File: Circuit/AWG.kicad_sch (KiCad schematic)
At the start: 24 parts, among them J1 Power, J2 Pump 1, J3 Pump 2, M1 Fan 1, M2 Fan 2, Q1 FQPF47P06, SW1 Switch, U1 R-78E5.0-0.5, U2 LM393

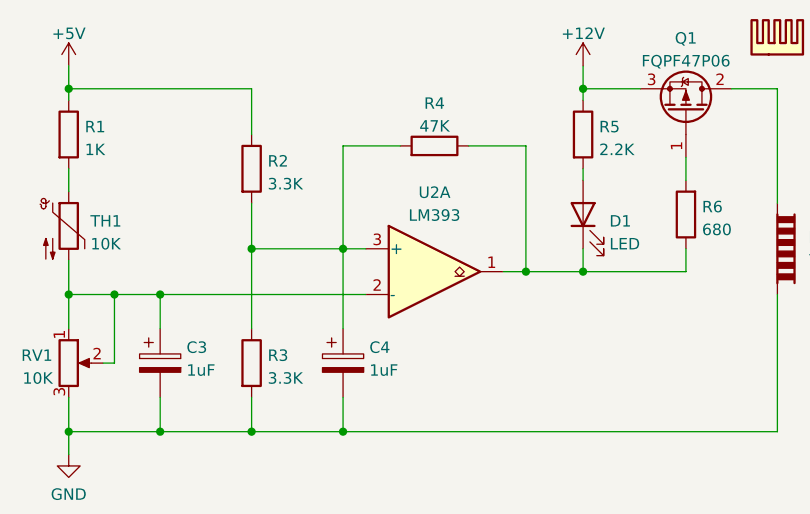
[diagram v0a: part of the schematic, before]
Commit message: [Circuit] Change a resistor to a potentiometer to adjust upper bound of the switching
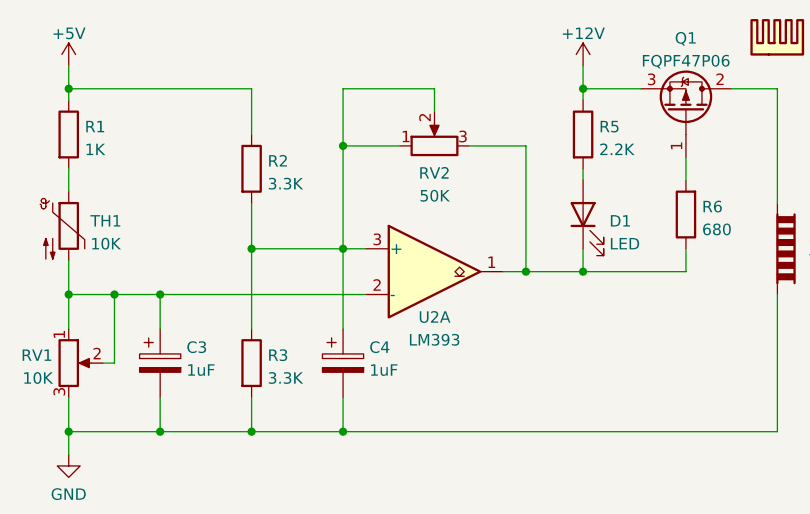
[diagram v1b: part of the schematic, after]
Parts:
- removed R4: 47K, Resistor_THT:R_Axial_DIN0207_L6.3mm_D2.5mm_P7.62mm_Horizontal, symbol Device:R
- added RV2: 50K, Potentiometer_THT:Potentiometer_Bourns_3339P_Vertical, symbol Device:R_Potentiometer
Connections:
- net at D1.1 (K), R6.1, U2.1: now also RV2.3
- net at C4.1, R2.2, R3.1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: now also RV2.1, RV2.2
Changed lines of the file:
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@@
   (junction (at 195.58 58.42) (diameter 0) (color 0 0 0 0)
+  )
+  (junction (at 175.26 44.45) (diameter 0) (color 0 0 0 0)
   )
   (junction (at 144.78 38.1) (diameter 0) (color 0 0 0 0)
@@
     (stroke (width 0) (type default) (color 0 0 0 0))
   )
+  (wire (pts (xy 185.42 38.1) (xy 175.26 38.1))
+    (stroke (width 0) (type default) (color 0 0 0 0))
+  )
   (wire (pts (xy 69.85 118.11) (xy 64.77 118.11))
     (stroke (width 0) (type default) (color 0 0 0 0))
@@
     (stroke (width 0) (type default) (color 0 0 0 0))
   )
+  (wire (pts (xy 185.42 40.64) (xy 185.42 38.1))
+    (stroke (width 0) (type default) (color 0 0 0 0))
+  )
   (wire (pts (xy 218.44 38.1) (xy 223.52 38.1))
     (stroke (width 0) (type default) (color 0 0 0 0))
@@
   )
   (wire (pts (xy 144.78 35.56) (xy 144.78 38.1))
+    (stroke (width 0) (type default) (color 0 0 0 0))
+  )
+  (wire (pts (xy 175.26 38.1) (xy 175.26 44.45))
     (stroke (width 0) (type default) (color 0 0 0 0))
   )
@@
     (pin "2")
   )
-  (symbol (lib_id "Device:R") (at 185.42 44.45 270) (mirror x) (unit 1)
-    (in_bom yes) (on_board yes) (fields_autoplaced)
-    (property "Reference" "R4" (id 0) (at 185.42 39.7342 90))
-    (property "Value" "47K" (id 1) (at 185.42 42.2711 90))
-    (property "Footprint" "Resistor_THT:R_Axial_DIN0207_L6.3mm_D2.5mm_P7.62mm_Horizontal" (id 2) (at 185.42 46.228 90)
-      (effects (font (size 1.27 1.27)) hide)
-    )
-    (property "Datasheet" "~" (id 3) (at 185.42 44.45 0)
-      (effects (font (size 1.27 1.27)) hide)
-    )
-    (pin "1")
-    (pin "2")
-  )
   (symbol (lib_id "Device:C_Polarized") (at 83.82 59.69 0) (mirror y) (unit 1)
     (in_bom yes) (on_board yes)
@@
   )
   (symbol (lib_id "Comparator:LM393") (at 185.42 58.42 0) (unit 1)
-    (in_bom yes) (on_board yes) (fields_autoplaced)
-    (property "Reference" "U2" (id 0) (at 185.42 49.6402 0))
-    (property "Value" "LM393" (id 1) (at 185.42 52.1771 0))
+    (in_bom yes) (on_board yes)
+    (property "Reference" "U2" (id 0) (at 185.42 63.5031 0))
+    (property "Value" "LM393" (id 1) (at 185.42 66.04 0))
     (property "Footprint" "Package_DIP:DIP-8_W7.62mm_Socket" (id 2) (at 185.42 58.42 0)
       (effects (font (size 1.27 1.27)) hide)
@@
     (pin "2")
   )
+  (symbol (lib_id "Device:R_Potentiometer") (at 185.42 44.45 90) (unit 1)
+    (in_bom yes) (on_board yes) (fields_autoplaced)
+    (property "Reference" "RV2" (id 0) (at 185.42 47.4964 90))
+    (property "Value" "50K" (id 1) (at 185.42 50.0333 90))
+    (property "Footprint" "Potentiometer_THT:Potentiometer_Bourns_3339P_Vertical" (id 2) (at 185.42 44.45 0)
+      (effects (font (size 1.27 1.27)) hide)
+    )
+    (property "Datasheet" "~" (id 3) (at 185.42 44.45 0)
+      (effects (font (size 1.27 1.27)) hide)
+    )
+    (pin "1")
+    (pin "2")
+    (pin "3")
+  )
   (sheet_instances
     (path "/" (page "1"))
@@
       (reference "R3") (unit 1) (value "3.3K") (footprint "Resistor_THT:R_Axial_DIN0207_L6.3mm_D2.5mm_P7.62mm_Horizontal")
     )
-    (path "/1870fe66-613a-4315-8238-19d41d32004b"
-      (reference "R4") (unit 1) (value "47K") (footprint "Resistor_THT:R_Axial_DIN0207_L6.3mm_D2.5mm_P7.62mm_Horizontal")
-    )
     (path "/22d073f7-e4a0-4cd4-a3b1-cf11aea04c7d"
       (reference "R5") (unit 1) (value "2.2K") (footprint "Resistor_THT:R_Axial_DIN0207_L6.3mm_D2.5mm_P7.62mm_Horizontal")
@@
       (reference "RV1") (unit 1) (value "10K") (footprint "Potentiometer_THT:Potentiometer_Bourns_3339P_Vertical")
     )
+    (path "/fe02be9d-6a84-4770-83b0-5b2bf60db1ec"
+      (reference "RV2") (unit 1) (value "50K") (footprint "Potentiometer_THT:Potentiometer_Bourns_3339P_Vertical")
+    )
     (path "/941be606-5dae-46f1-be50-e2701a32a3aa"

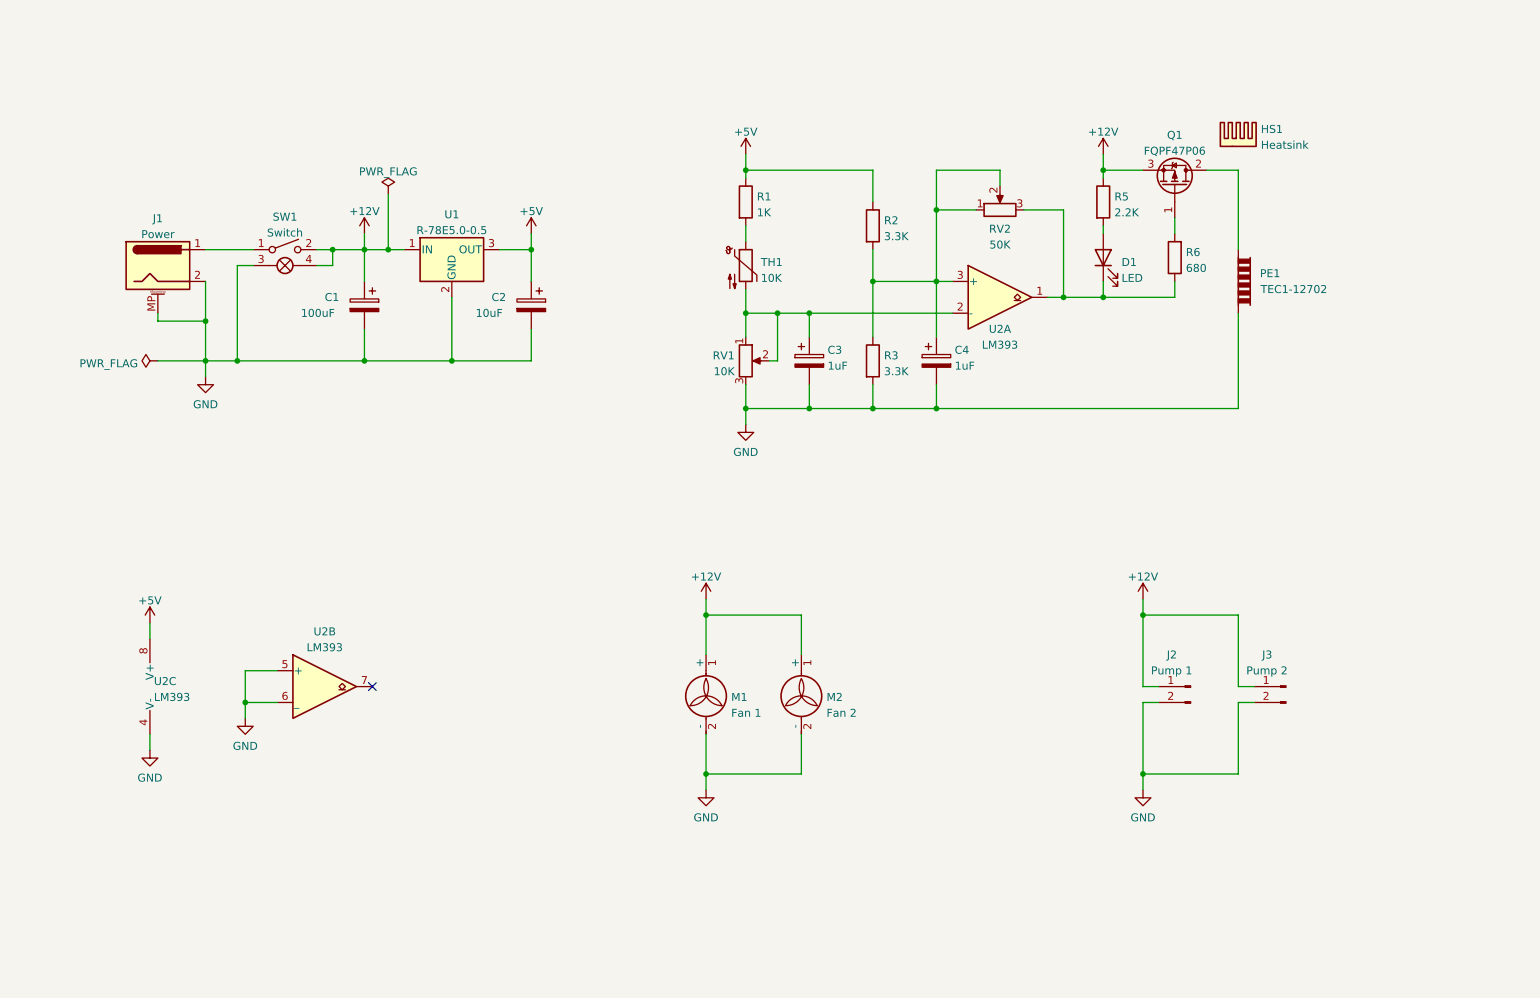
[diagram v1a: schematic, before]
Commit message: [Circuit] Redesign the control module, use an Arduino as the computation core
Related issue #6
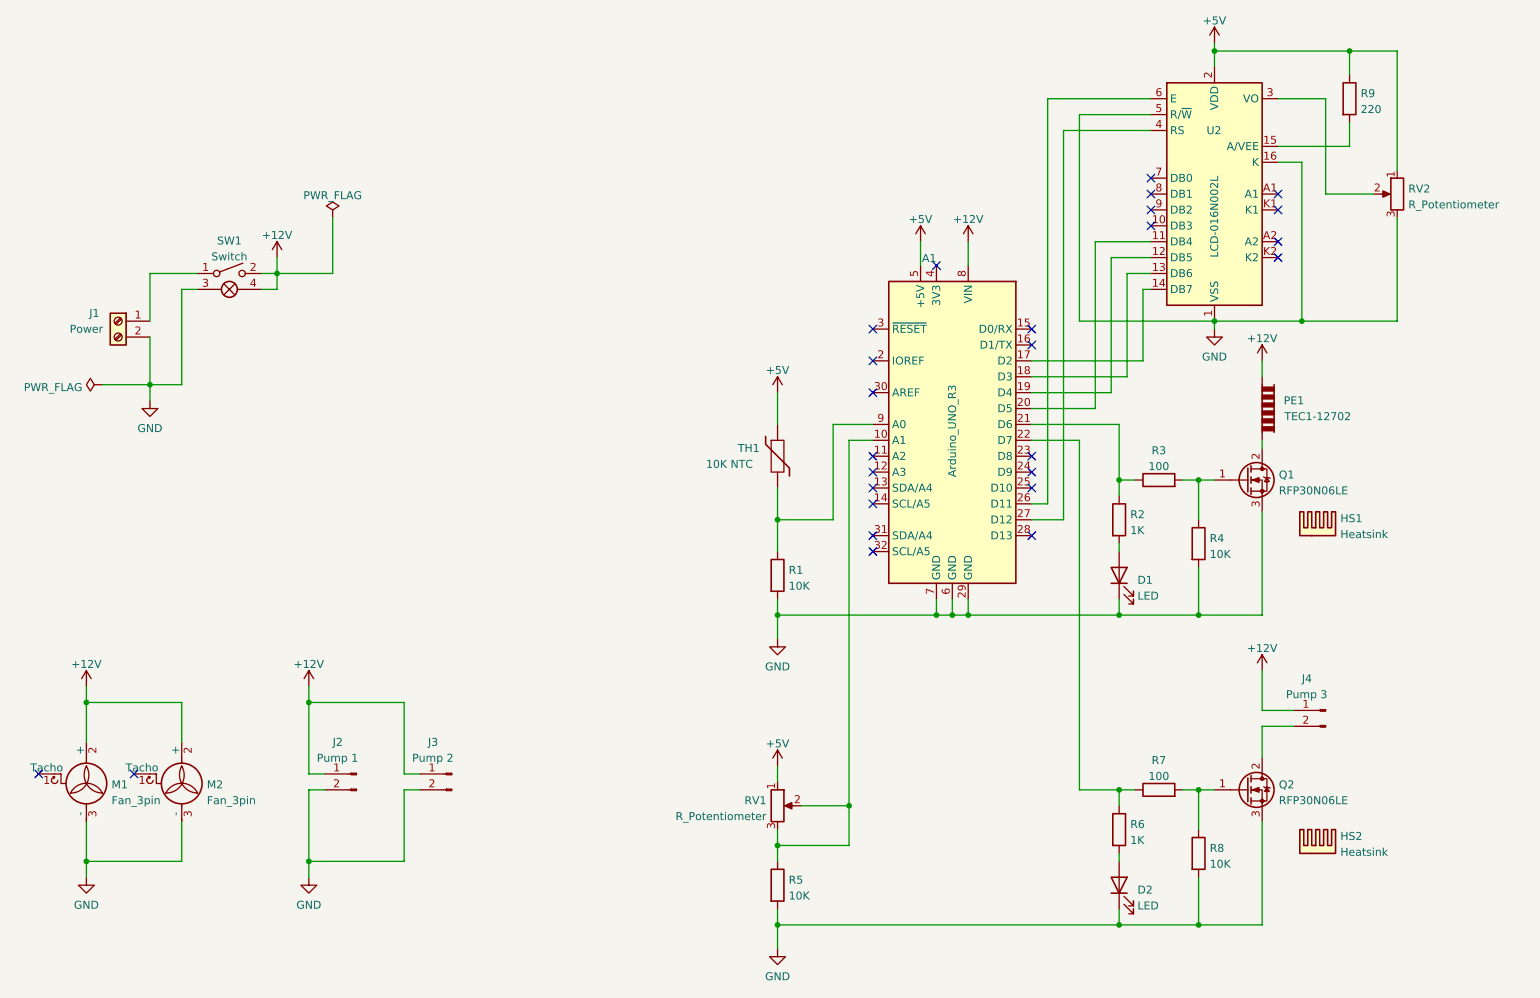
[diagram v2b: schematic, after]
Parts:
- removed C1: 100uF, Capacitor_THT:CP_Radial_D6.3mm_P2.50mm, symbol Device:C_Polarized
- removed C2: 10uF, Capacitor_THT:CP_Radial_D4.0mm_P1.50mm, symbol Device:C_Polarized
- removed C3, C4: 1uF, Capacitor_THT:CP_Radial_D4.0mm_P1.50mm, symbol Device:C_Polarized
- removed J1: Power, Connector_BarrelJack:BarrelJack_Wuerth_6941xx301002, symbol Connector:Barrel_Jack_MountingPin
- removed M1: Fan 1, Connector_JST:JST_XH_B2B-XH-A_1x02_P2.50mm_Vertical, symbol Motor:Fan
- removed M2: Fan 2, Connector_JST:JST_XH_B2B-XH-A_1x02_P2.50mm_Vertical, symbol Motor:Fan
- removed Q1: FQPF47P06, Package_TO_SOT_THT:TO-220-3_Vertical, symbol Device:Q_PMOS_GDS
- removed TH1: 10K, Connector_PinHeader_2.54mm:PinHeader_1x02_P2.54mm_Vertical, symbol Device:Thermistor_NTC
- removed U1: R-78E5.0-0.5, Converter_DCDC:Converter_DCDC_RECOM_R-78E-0.5_THT, symbol Regulator_Switching:R-78E5.0-0.5
- removed U2: LM393, Package_DIP:DIP-8_W7.62mm_Socket, symbol Comparator:LM393
- added A1: Arduino_UNO_R3, Module:Arduino_UNO_R3, symbol MCU_Module:Arduino_UNO_R3
- added D2: LED, LED_THT:LED_D3.0mm_FlatTop, symbol Device:LED
- added HS2: Heatsink, AWG:Heatsink_TO220_15x10mm, symbol Mechanical:Heatsink
- added J1: Power, TerminalBlock:TerminalBlock_bornier-2_P5.08mm, symbol Connector:Screw_Terminal_01x02
- added J4: Pump 3, Connector_PinHeader_2.54mm:PinHeader_1x02_P2.54mm_Vertical, symbol Connector:Conn_01x02_Male
- added M1, M2: Fan_3pin, Connector_PinHeader_2.54mm:PinHeader_1x03_P2.54mm_Vertical, symbol Motor:Fan_3pin
- added Q1, Q2: RFP30N06LE, Package_TO_SOT_THT:TO-220-3_Vertical, symbol Device:Q_NMOS_GDS
- added R4, R8: 10K, Resistor_THT:R_Axial_DIN0207_L6.3mm_D2.5mm_P7.62mm_Horizontal, symbol Device:R
- added R7: 100, Resistor_THT:R_Axial_DIN0207_L6.3mm_D2.5mm_P7.62mm_Horizontal, symbol Device:R
- added R9: 220, Resistor_THT:R_Axial_DIN0207_L6.3mm_D2.5mm_P7.62mm_Horizontal, symbol Device:R
- added TH1: 10K NTC, Connector_PinHeader_2.54mm:PinHeader_1x02_P2.54mm_Vertical, symbol Device:Thermistor
- added U2: LCD-016N002L, Display:LCD-016N002L, symbol Display_Character:LCD-016N002L
- J2, J3: footprint Connector_JST:JST_XH_B2B-XH-A_1x02_P2.50mm_Vertical -> Connector_PinHeader_2.54mm:PinHeader_1x02_P2.54mm_Vertical
- PE1: footprint Connector_JST:JST_XH_B2B-XH-A_1x02_P2.50mm_Vertical -> TerminalBlock:TerminalBlock_bornier-2_P5.08mm
- R1: value 1K -> 10K
- R2: value 3.3K -> 1K
- R3: value 3.3K -> 100
- R5: value 2.2K -> 10K
- R6: value 680 -> 1K
- RV1: value 10K -> R_Potentiometer; footprint Potentiometer_THT:Potentiometer_Bourns_3339P_Vertical -> (none)
- RV2: value 50K -> R_Potentiometer; footprint Potentiometer_THT:Potentiometer_Bourns_3339P_Vertical -> (none)
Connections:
- net +12V: now also PE1.2, A1.8 (VIN), J4.1 (Pin_1), M1.2 (+), M2.2 (+); no longer R5.1
- net +5V: now also RV1.1, RV2.1, A1.5 (+5V), R9.1, TH1.1, U2.2 (VDD); no longer R1.1, R2.1
- net GND: now also D1.1 (K), R1.2, R5.2, RV2.3, A1.29 (GND), A1.6 (GND), A1.7 (GND), D2.1 (K), J1.2 (Pin_2), M1.3 (-), M2.3 (-), Q1.3 (S), Q2.3 (S), R4.2, R8.2, U2.1 (VSS), U2.16 (K), U2.5 (R/~{W}); no longer PE1.2, R3.2, RV1.3
- net at D1.2 (A): now also R2.2; no longer R5.2
- net at SW1.1: now also J1.1 (Pin_1)
- net at PE1.1: now also Q1.2 (D)
- net at RV1.2: now also R5.1, RV1.3, A1.10 (A1); no longer RV1.1
- net at R6.2: now also D2.2 (A)
- new net: A1.17 (D2), U2.14 (DB7)
- new net: A1.18 (D3), U2.13 (DB6)
- new net: A1.19 (D4), U2.12 (DB5)
- new net: A1.20 (D5), U2.11 (DB4)
- new net: A1.21 (D6), R2.1, R3.1
- new net: A1.22 (D7), R6.1, R7.1
- new net: A1.26 (D11), U2.6 (E)
- new net: A1.27 (D12), U2.4 (RS)
- new net: A1.9 (A0), R1.1, TH1.2
- new net: Q1.1 (G), R3.2, R4.1
- new net: J4.2 (Pin_2), Q2.2 (D)
- new net: Q2.1 (G), R7.2, R8.1
- new net: R9.2, U2.15 (A/VEE)
- new net: RV2.2, U2.3 (VO)
- no-connect marks 1 -> 26

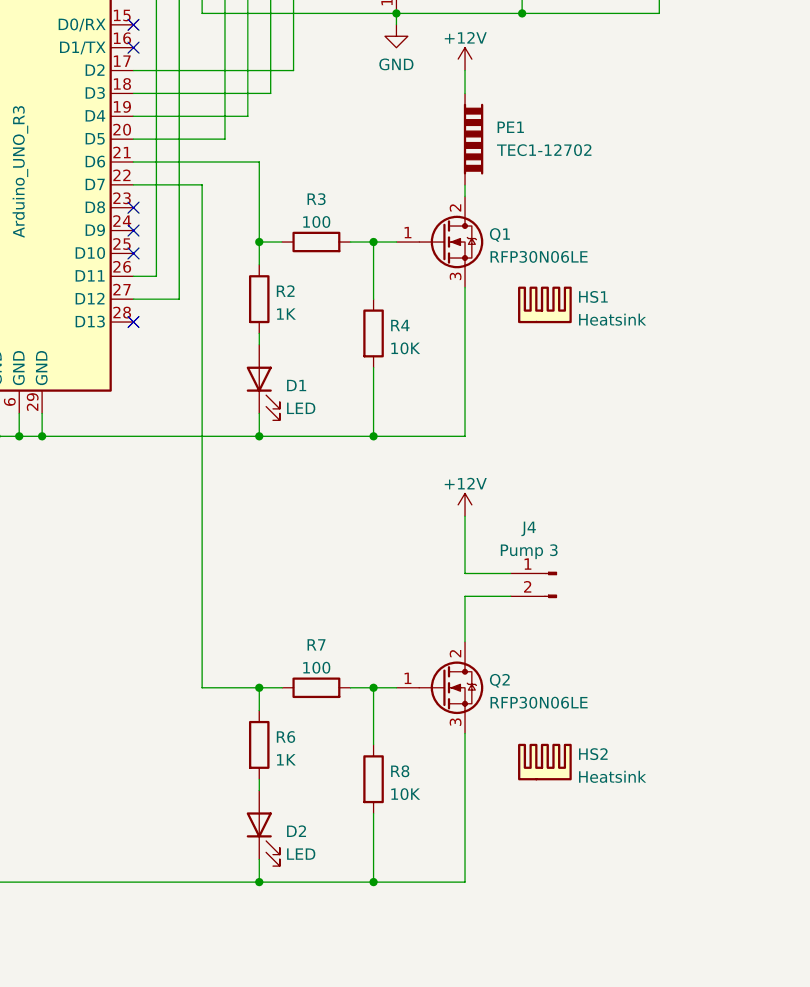
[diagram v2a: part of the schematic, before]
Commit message: [Circuit] Adjust the mosfet part in the circuit
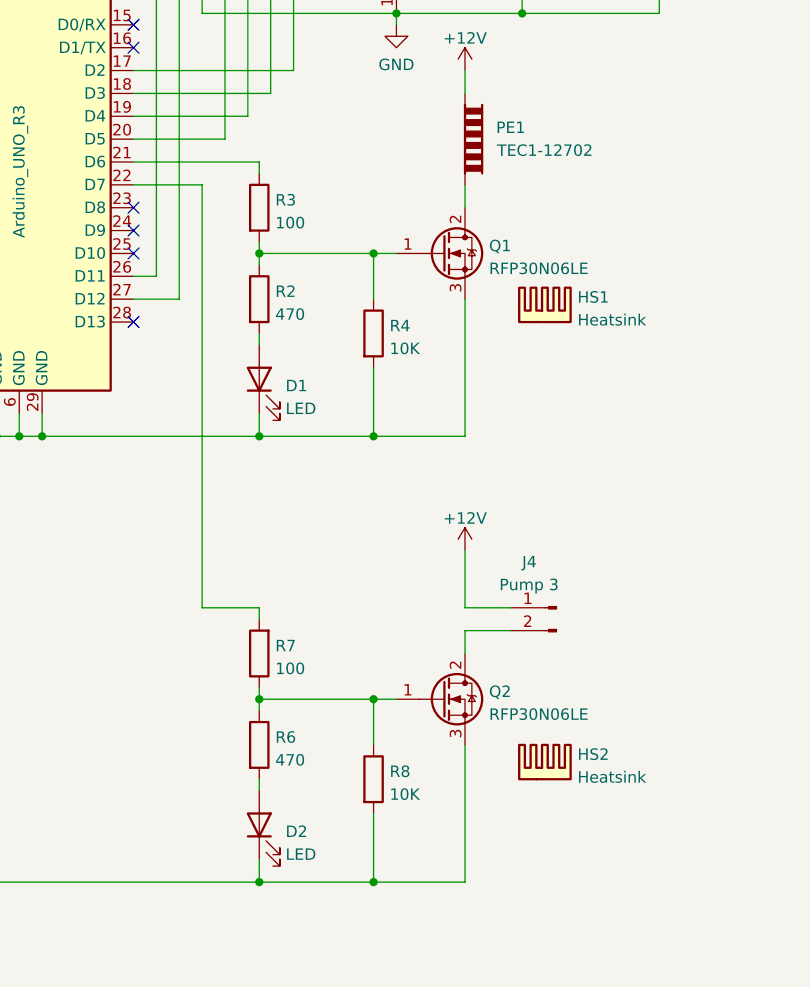
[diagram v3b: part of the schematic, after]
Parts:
- R2, R6: value 1K -> 470
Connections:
- net at A1.21 (D6), R3.1: no longer R2.1
- net at R6.1, R7.1: now also Q2.1 (G), R8.1; no longer A1.22 (D7)
- net at Q1.1 (G), R3.2, R4.1: now also R2.1
- new net: A1.22 (D7), R7.2
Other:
- moved on the sheet: J4, Q1, Q2, R3, R7
